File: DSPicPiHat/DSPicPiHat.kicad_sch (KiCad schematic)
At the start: 56 parts

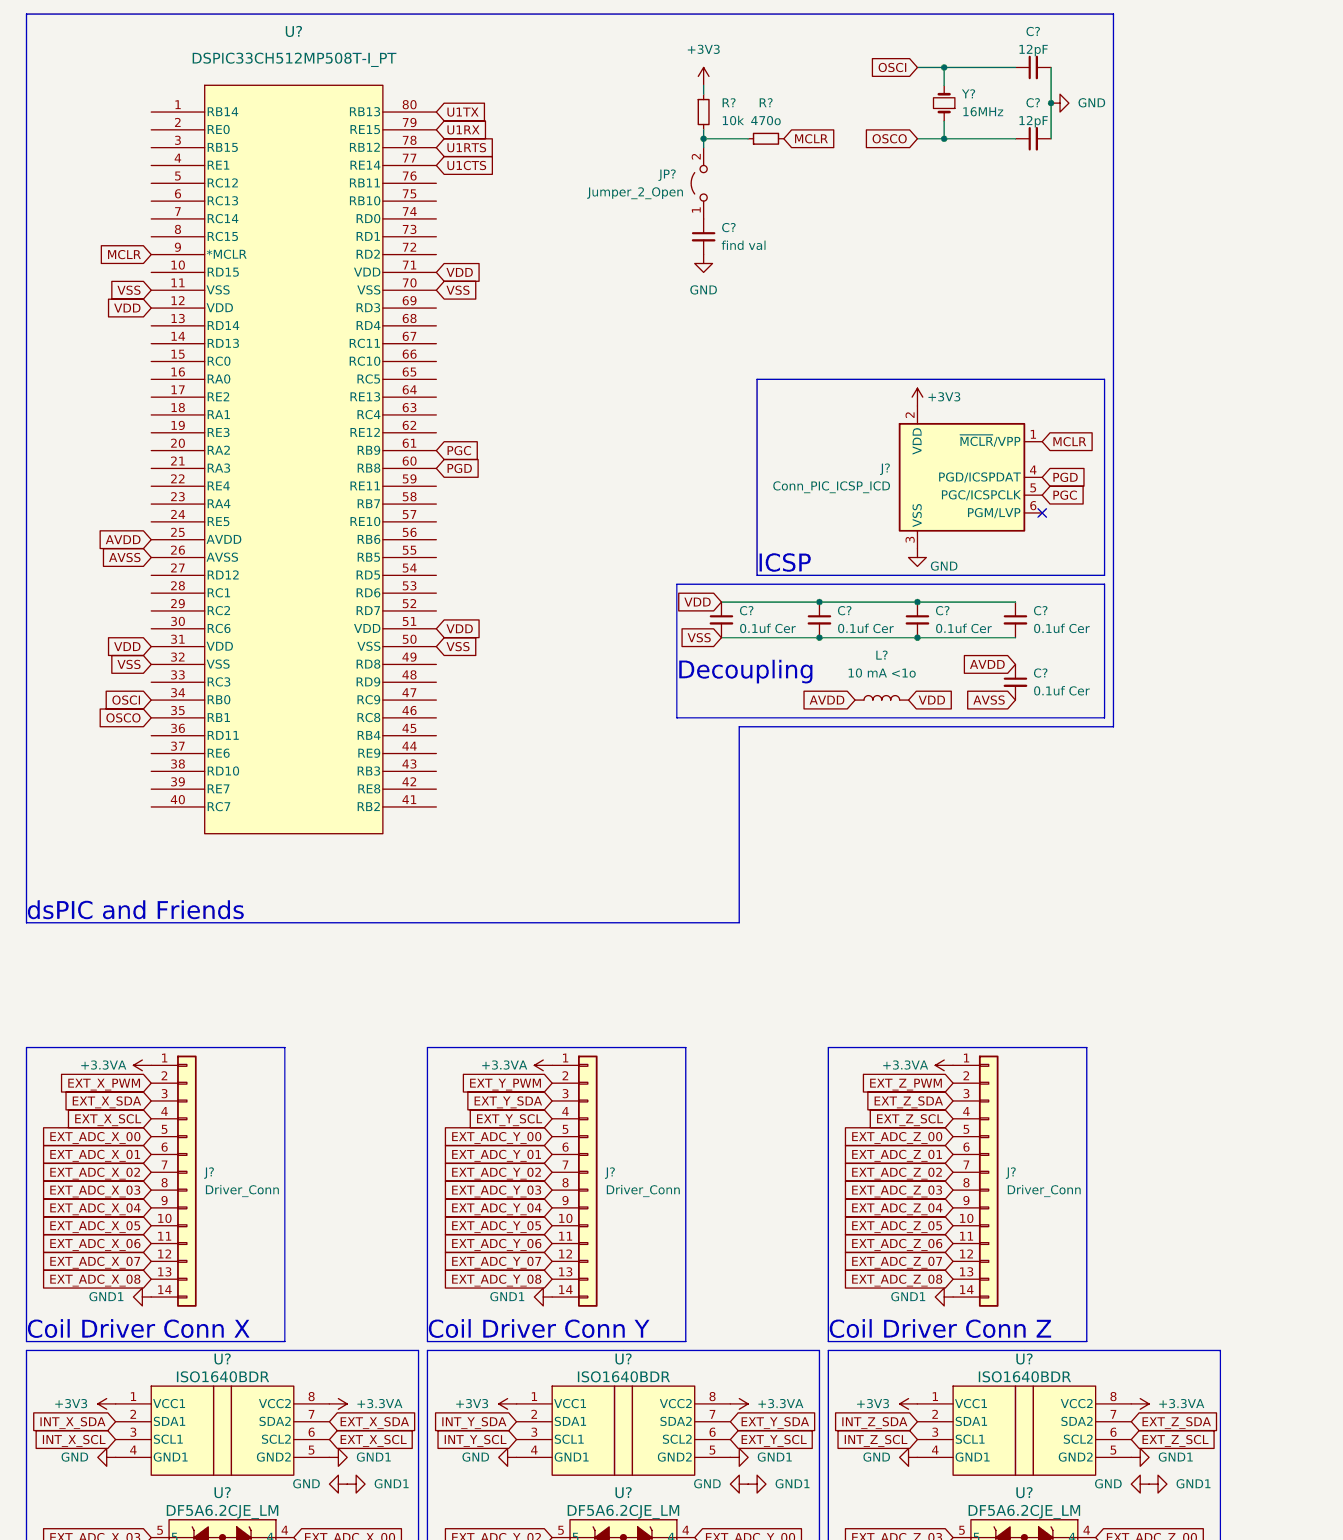
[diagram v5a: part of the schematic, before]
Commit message: added leds to coil connector plugs
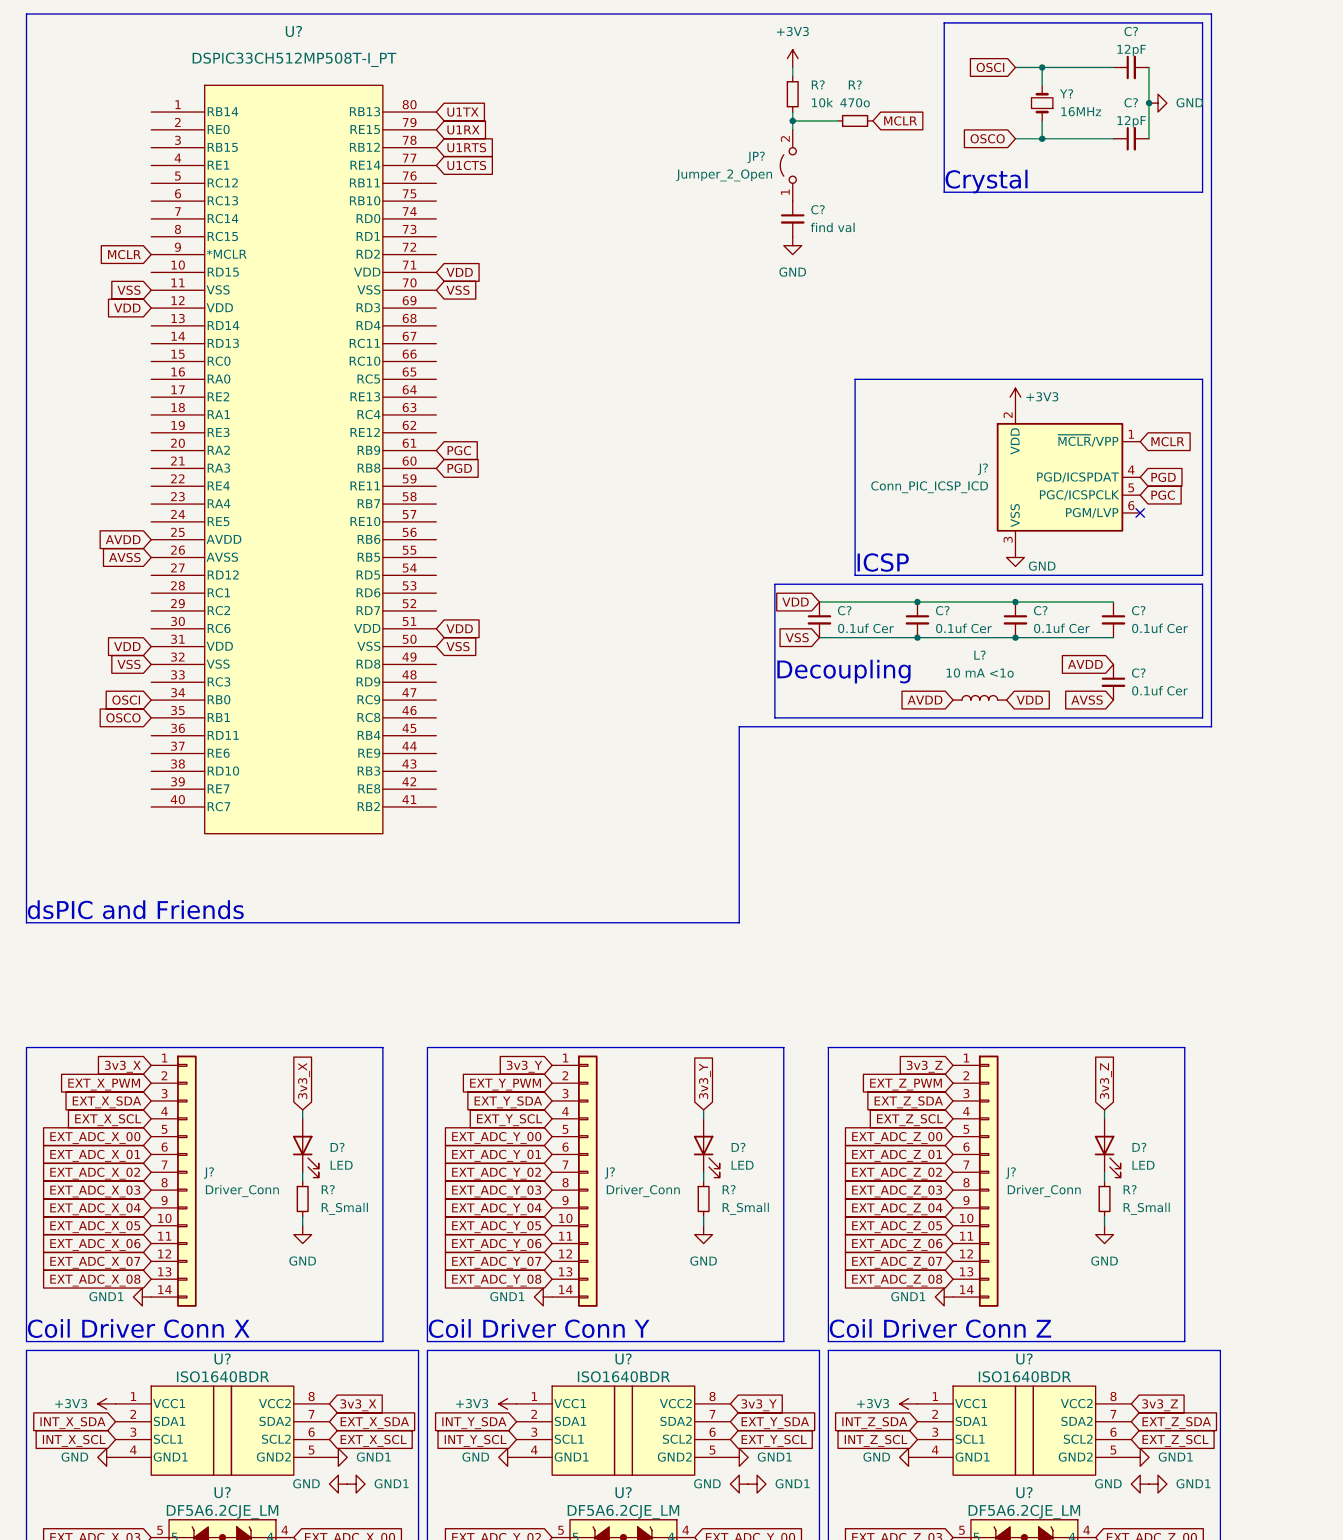
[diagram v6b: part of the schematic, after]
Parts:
- added D? (x3): LED, symbol Device:LED
- added R? (x3): R_Small, symbol Device:R_Small
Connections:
- net +3.3VA: no longer J?.1 (Pin_1), J?.1 (Pin_1), J?.1 (Pin_1), U?.8 (VCC2), U?.8 (VCC2), U?.8 (VCC2)
- net GND: now also R?.2, R?.2, R?.2
- new net: D?.1 (K), R?.1 (x3)
- new net 3v3_X: D?.2 (A), J?.1 (Pin_1), U?.8 (VCC2)
- new net 3v3_Y: D?.2 (A), J?.1 (Pin_1), U?.8 (VCC2)
- new net 3v3_Z: D?.2 (A), J?.1 (Pin_1), U?.8 (VCC2)
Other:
- note added: "Crystal"
- moved on the sheet: C?, J?, JP?, L?, R?, Y?

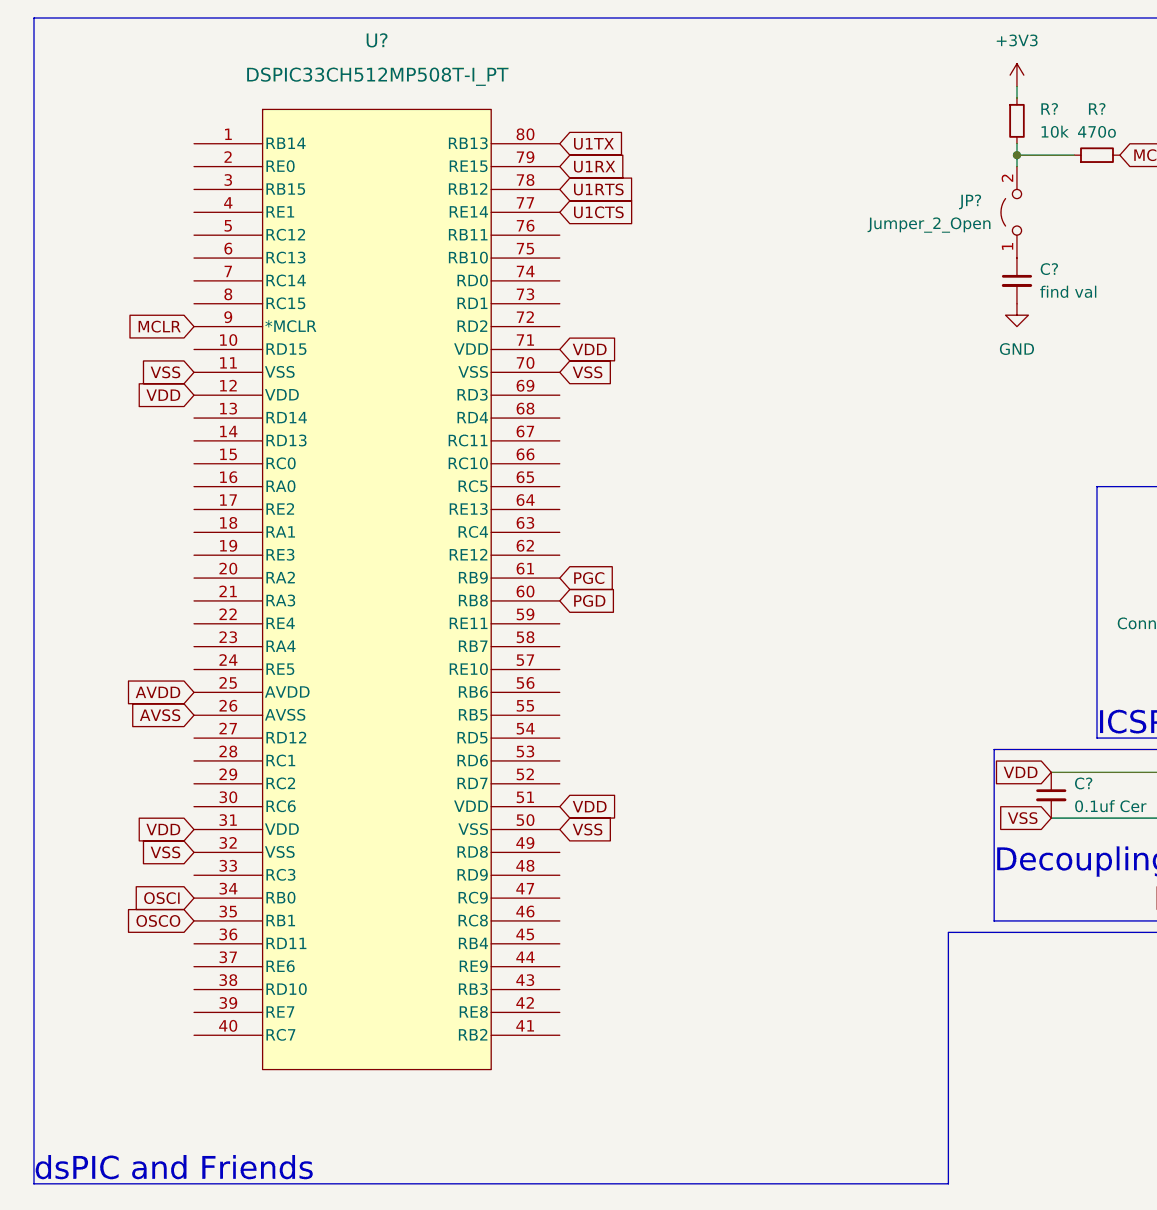
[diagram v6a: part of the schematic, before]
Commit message: wired up i2c, PWM, and ADC pins from connectors
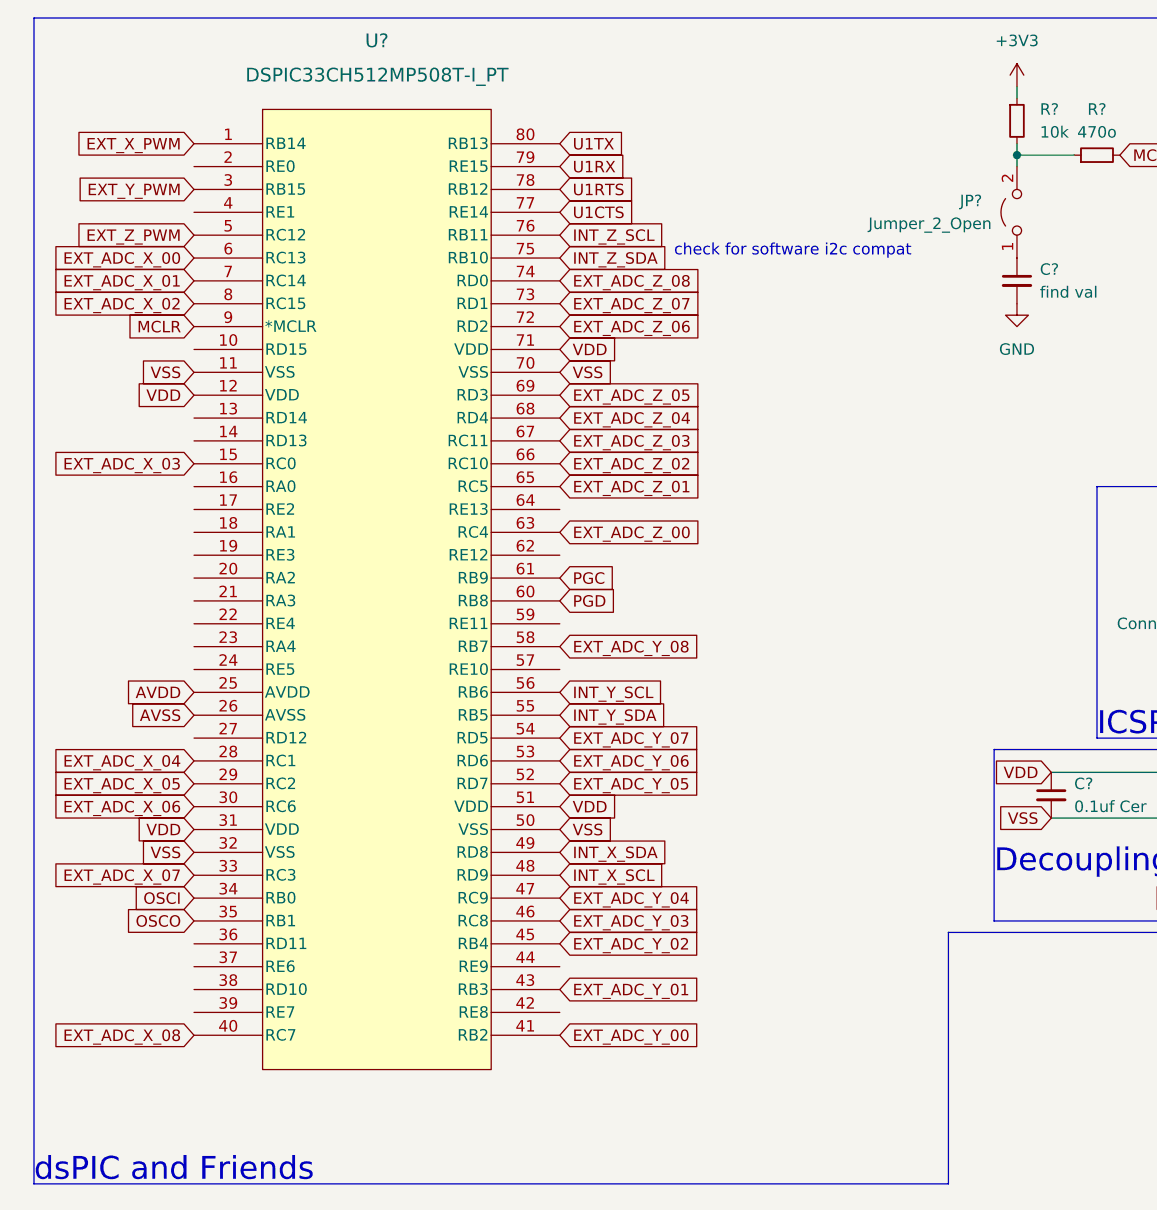
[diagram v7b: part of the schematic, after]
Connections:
- net EXT_ADC_X_00: now also U?.6 (RC13)
- net EXT_ADC_X_01: now also U?.7 (RC14)
- net EXT_ADC_X_02: now also U?.8 (RC15)
- net EXT_ADC_X_03: now also U?.15 (RC0)
- net EXT_ADC_X_04: now also U?.28 (RC1)
- net EXT_ADC_X_05: now also U?.29 (RC2)
- net EXT_ADC_X_06: now also U?.30 (RC6)
- net EXT_ADC_X_07: now also U?.33 (RC3)
- net EXT_ADC_X_08: now also U?.40 (RC7)
- net EXT_ADC_Y_00: now also U?.41 (RB2)
- net EXT_ADC_Y_01: now also U?.43 (RB3)
- net EXT_ADC_Y_02: now also U?.45 (RB4)
- net EXT_ADC_Y_03: now also U?.46 (RC8)
- net EXT_ADC_Y_04: now also U?.47 (RC9)
- net EXT_ADC_Y_05: now also U?.52 (RD7)
- net EXT_ADC_Y_06: now also U?.53 (RD6)
- net EXT_ADC_Y_07: now also U?.54 (RD5)
- net EXT_ADC_Y_08: now also U?.58 (RB7)
- net EXT_ADC_Z_00: now also U?.63 (RC4)
- net EXT_ADC_Z_01: now also U?.65 (RC5)
- net EXT_ADC_Z_02: now also U?.66 (RC10)
- net EXT_ADC_Z_03: now also U?.67 (RC11)
- net EXT_ADC_Z_04: now also U?.68 (RD4)
- net EXT_ADC_Z_05: now also U?.69 (RD3)
- net EXT_ADC_Z_06: now also U?.72 (RD2)
- net EXT_ADC_Z_07: now also U?.73 (RD1)
- net EXT_ADC_Z_08: now also U?.74 (RD0)
- net EXT_X_PWM: now also U?.1 (RB14)
- net EXT_Y_PWM: now also U?.3 (RB15)
- net EXT_Z_PWM: now also U?.5 (RC12)
- net INT_X_SCL: now also U?.48 (RD9)
- net INT_X_SDA: now also U?.49 (RD8)
- net INT_Y_SCL: now also U?.56 (RB6)
- net INT_Y_SDA: now also U?.55 (RB5)
- net INT_Z_SCL: now also U?.76 (RB11)
- net INT_Z_SDA: now also U?.75 (RB10)
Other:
- note added: "check for software i2c compat"

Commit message: dsPIC to Pi, dsPIC dip switches, dspic and Pi LEDs, and spi screen connectors.
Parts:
- added D? (x6): LED, symbol Device:LED
- added D? (x4): WS2812B, LED_SMD:LED_WS2812B_PLCC4_5.0x5.0mm_P3.2mm, symbol LED:WS2812B
- added J?: Nice!View, symbol Connector:Conn_01x05_Female
- added J?: GenericSPIconn, symbol Connector:Conn_01x08_Female
- added J?: GeneralSPIDisplay, symbol Connector:Conn_01x08_Female
- added R? (x6): R_Small, symbol Device:R_Small
- added R?: 470o, symbol Device:R_Small
- added RN?: 10k, Resistor_THT:R_Array_SIP9, symbol Device:R_Network08
- added SW?: SW_DIP_x08, symbol Switch:SW_DIP_x08
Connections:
- net +3V3: now also J?.1 (Pin_1), J?.3 (Pin_3), J?.7 (Pin_7)
- net +5V: now also D?.1 (VDD), D?.1 (VDD), D?.1 (VDD), D?.1 (VDD), J?.2 (Pin_2), RN?.1 (common)
- net GND: now also D?.3 (VSS), D?.3 (VSS), D?.3 (VSS), D?.3 (VSS), J?.1 (Pin_1), J?.2 (Pin_2), J?.4 (Pin_4), J?.8 (Pin_8), R?.2, R?.2, R?.2, R?.2, R?.2, R?.2, SW?.10, SW?.11, SW?.12, SW?.13, SW?.14, SW?.15, SW?.16, SW?.9
- net RST: now reaches J?.13 (Pin_13)
- net RST: now also J?.7 (Pin_7)
- net Backlight: now reaches J?.18 (Pin_18)
- net Backlight: now also J?.8 (Pin_8)
- net PI_MOSI: now reaches J?.19 (Pin_19)
- net PI_MOSI: now also U?.56 (RB6), J?.1 (Pin_1), J?.3 (Pin_3), J?.4 (Pin_4)
- net PI_MISO: now reaches J?.21 (Pin_21)
- net PI_MISO: now also U?.75 (RB10), J?.3 (Pin_3)
- net Data/Command: now reaches J?.22 (Pin_22)
- net Data/Command: now also J?.6 (Pin_6)
- net PI_SCLK: now reaches J?.23 (Pin_23)
- net PI_SCLK: now also U?.76 (RB11), J?.2 (Pin_2), J?.4 (Pin_4), J?.5 (Pin_5)
- net PI_CE0: now reaches J?.24 (Pin_24)
- net PI_CE0: now also U?.55 (RB5)
- net PI_CE1: now reaches J?.26 (Pin_26)
- net PI_CE1: now also J?.5 (Pin_5), J?.5 (Pin_5), J?.6 (Pin_6)
- net PI_NEOPIXEL: now reaches J?.32 (Pin_32)
- net PI_NEOPIXEL: now also R?.1
- net DIP_00: now reaches U?.16 (RA0)
- net DIP_00: now also RN?.9 (R8), SW?.1
- net DIP_01: now reaches U?.17 (RE2)
- net DIP_01: now also RN?.8 (R7), SW?.2
- net DIP_02: now reaches U?.18 (RA1)
- net DIP_02: now also RN?.7 (R6), SW?.3
- net DIP_03: now reaches U?.19 (RE3)
- net DIP_03: now also RN?.6 (R5), SW?.4
- net DIP_04: now reaches U?.20 (RA2)
- net DIP_04: now also RN?.5 (R4), SW?.5
- net DIP_05: now reaches U?.21 (RA3)
- net DIP_05: now also RN?.4 (R3), SW?.6
- net DIP_06: now reaches U?.22 (RE4)
- net DIP_06: now also RN?.3 (R2), SW?.7
- net DIP_07: now reaches U?.23 (RA4)
- net DIP_07: now also RN?.2 (R1), SW?.8
- net dsPIC_LED_00: now reaches U?.36 (RD11)
- net dsPIC_LED_00: now also D?.2 (A)
- net dsPIC_LED_01: now reaches U?.37 (RE6)
- net dsPIC_LED_01: now also D?.2 (A)
- net dsPIC_LED_02: now reaches U?.38 (RD10)
- net dsPIC_LED_02: now also D?.2 (A)
- net dsPIC_LED_03: now reaches U?.39 (RE7)
- net dsPIC_LED_03: now also D?.2 (A)
- net dsPIC_LED_04: now reaches U?.42 (RE8)
- net dsPIC_LED_04: now also D?.2 (A)
- net dsPIC_LED_05: now reaches U?.44 (RE9)
- net dsPIC_LED_05: now also D?.2 (A)
- net INT_X_SCL renamed INT_SCL
- net INT_SCL: now also U?.3 (SCL1), U?.3 (SCL1)
- net INT_X_SDA renamed INT_SDA
- net INT_SDA: now also U?.2 (SDA1), U?.2 (SDA1)
- removed net INT_Y_SCL: U?.3 (SCL1), U?.56 (RB6)
- removed net INT_Y_SDA: U?.2 (SDA1), U?.55 (RB5)
- removed net INT_Z_SCL: U?.3 (SCL1), U?.76 (RB11)
- removed net INT_Z_SDA: U?.2 (SDA1), U?.75 (RB10)
- new net: D?.1 (K), R?.1 (x6)
- new net: D?.2 (DOUT), D?.4 (DIN) (x3)
- new net: D?.4 (DIN), R?.2
- no-connect marks 7 -> 8
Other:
- note added: "DIP switches"
- note added: "Pi NeoPixel"
- note added: "Screen and SPI conns"
- note added: "dsPIC LEDs"
- note removed: "check for software i2c compat"
- moved on the sheet: J?
